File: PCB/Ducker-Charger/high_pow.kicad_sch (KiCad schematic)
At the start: 27 parts, among them Q1 NCE3080K, Q2 NCE3080K, Q3 NCE3080K, Q4 NCE3080K, U1 IP5389_CN_AACD_WC4QD

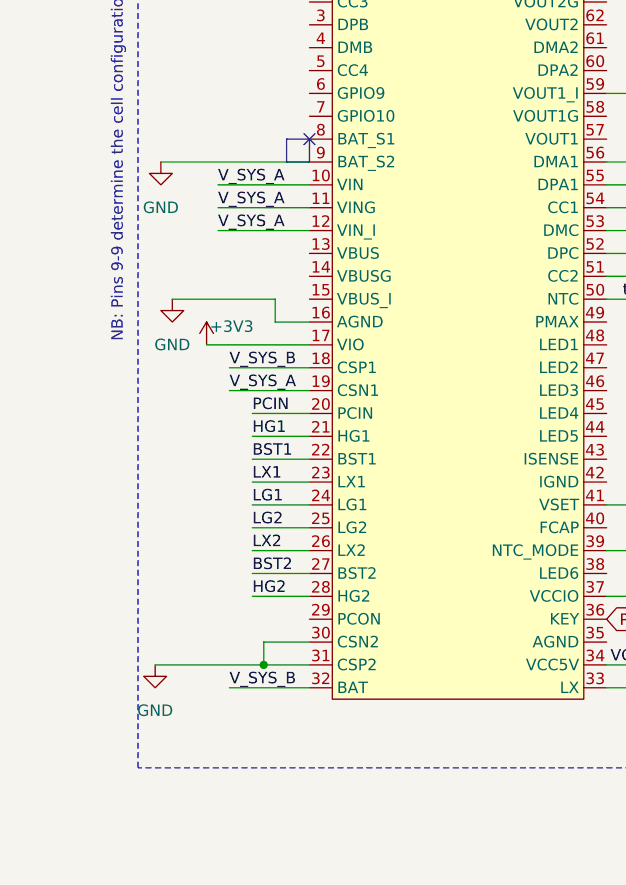
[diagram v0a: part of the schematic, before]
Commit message: feat: started BMS configuration
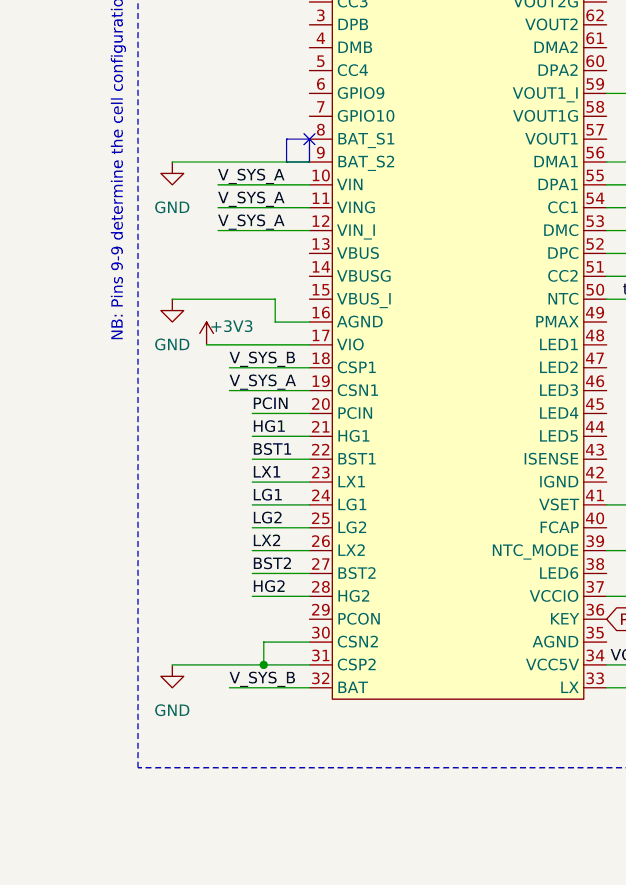
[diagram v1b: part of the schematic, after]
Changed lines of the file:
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@@
 	(wire
 		(pts
-			(xy 29.845 123.19) (xy 41.91 123.19)
+			(xy 31.75 123.19) (xy 41.91 123.19)
 		)
 		(stroke
@@
 	(wire
 		(pts
-			(xy 30.48 67.31) (xy 46.99 67.31)
+			(xy 31.75 67.31) (xy 46.99 67.31)
 		)
 		(stroke
@@
 	(symbol
 		(lib_id "power:GND")
-		(at 30.48 67.31 0)
+		(at 31.75 67.31 0)
 		(mirror y)
 		(unit 1)
@@
 		(fields_autoplaced yes)
 		(property "Reference" "#PWR018"
-			(at 30.48 73.66 0)
+			(at 31.75 73.66 0)
 			(effects
 				(font
@@
 		)
 		(property "Value" "GND"
-			(at 30.48 72.39 0)
+			(at 31.75 72.39 0)
 			(effects
 				(font
@@
 		)
 		(property "Footprint" ""
-			(at 30.48 67.31 0)
+			(at 31.75 67.31 0)
 			(effects
 				(font
@@
 		)
 		(property "Datasheet" ""
-			(at 30.48 67.31 0)
+			(at 31.75 67.31 0)
 			(effects
 				(font
@@
 		)
 		(property "Description" "Power symbol creates a global label with name \"GND\" , ground"
-			(at 30.48 67.31 0)
+			(at 31.75 67.31 0)
 			(effects
 				(font
@@
 	(symbol
 		(lib_id "power:GND")
-		(at 29.845 123.19 0)
+		(at 31.75 123.19 0)
 		(mirror y)
 		(unit 1)
@@
 		(fields_autoplaced yes)
 		(property "Reference" "#PWR019"
-			(at 29.845 129.54 0)
+			(at 31.75 129.54 0)
 			(effects
 				(font
@@
 		)
 		(property "Value" "GND"
-			(at 29.845 128.27 0)
+			(at 31.75 128.27 0)
 			(effects
 				(font
@@
 		)
 		(property "Footprint" ""
-			(at 29.845 123.19 0)
+			(at 31.75 123.19 0)
 			(effects
 				(font
@@
 		)
 		(property "Datasheet" ""
-			(at 29.845 123.19 0)
+			(at 31.75 123.19 0)
 			(effects
 				(font
@@
 		)
 		(property "Description" "Power symbol creates a global label with name \"GND\" , ground"
-			(at 29.845 123.19 0)
-			(effects
-				(font
+			(at 31.75 123.19 0)
+			(effects
+				(font

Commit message: feat: substituted IP5389 with BQ25713 + TPS25750
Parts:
- removed C_BST1, C_BST2: 100n, symbol Device:C
- removed R7: 51K, symbol Device:R
- removed TH1: Thermistor_NTC, symbol Device:Thermistor_NTC
- removed U1: IP5389_CN_AACD_WC4QD, EasyEDA:QFN-64_L8.0-W8.0-P0.40-TL-EP6.2, symbol EasyEDA:IP5389_CN_AACD_WC4QD
- added C32: 4.7u, symbol Device:C
- added C33: 1u, symbol Device:C
- added U7: TPS25750DRJKR, EasyEDA:QFN-38_L6.0-W4.0-P0.40-TL-EP_RJK, symbol EasyEDA:TPS25750DRJKR
- added U8: BQ25713RSNR, EasyEDA:QFN-32_L4.0-W4.0-P0.40-TL-EP2.8, symbol EasyEDA:BQ25713RSNR
- C1: value 10u -> 100n
- R2: value 27K -> 10
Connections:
- net GND: now also C32.2, C33.2, U8.27 (PGND), U8.33 (EP); no longer C1.2, C8.2, R2.2
- net SCL: now also U8.13 (SCL)
- net SDA: now also U8.12 (SDA)
- net VBUS: now also U8.1 (VBUS)
- net V_SYS_A: now also U8.20 (SRP), U8.22 (VSYS)
- net V_SYS_B: now also U8.19 (SRN)
- net CONF_SETT renamed REGN
- net REGN: now also C32.1, U8.28 (REGN)
- net HG1 renamed HIDRV2
- net HIDRV2: now also U8.24 (HIDRV2)
- net HG2 renamed HIDRV1
- net HIDRV1: now also U8.31 (HIDRV1)
- net LG1 renamed LODRV2
- net LODRV2: now also U8.26 (LODRV2)
- net LG2 renamed LODRV1
- net LODRV1: now also U8.29 (LODRV1)
- net LX1 renamed SW2
- net SW2: now also C8.2, U8.23 (SW2)
- net LX2 renamed SW1
- net SW1: now also C1.2, U8.32 (SW1)
- net PCIN renamed BTST2
- net BTST2: now also U8.25 (BTST2)
- net VCC5V renamed BTST1
- net BTST1: now also U8.30 (BTST1)
- new net VDDA: C33.1, R2.2, U8.7 (VDDA)
- no-connect marks 2 -> 1
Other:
- note removed: "BOOTSTRAP & DECOUPLING"
- note removed: "HARDWARE CONFIG"
- note removed: "HARDWARE SAFETY"
- note removed: "NB: Pins 9-9 determine the cell configuration"
- note removed: "pullup must be added 4k7 - 3v3"

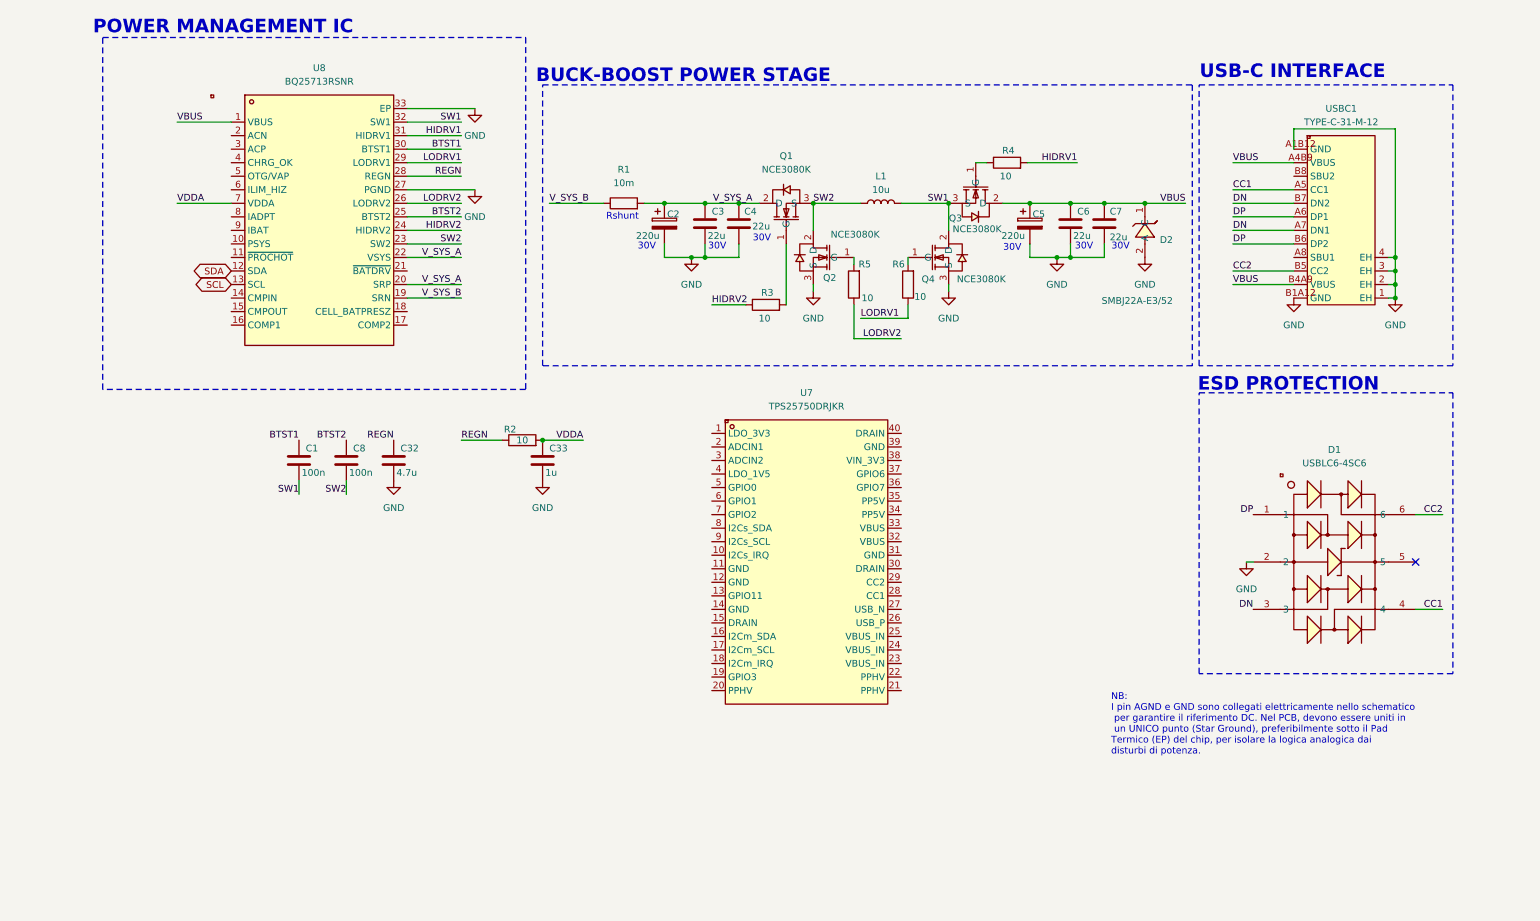
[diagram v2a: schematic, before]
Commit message: feat: completed BQ25713 + TPS25750 config
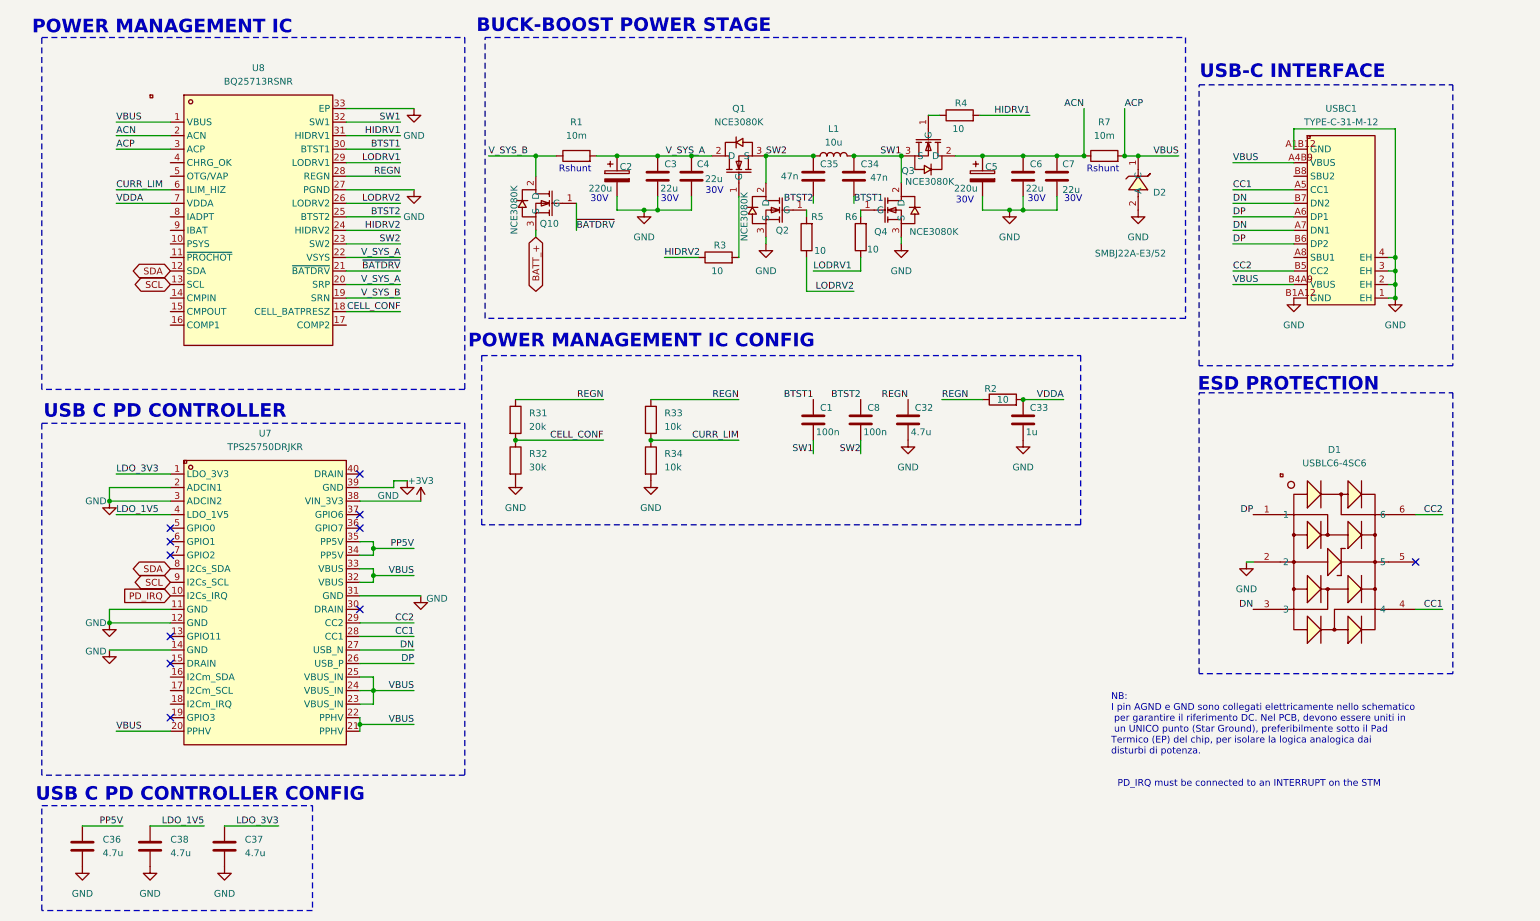
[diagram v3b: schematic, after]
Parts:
- added C34, C35: 47n, symbol Device:C
- added C36, C37, C38: 4.7u, symbol Device:C
- added Q10: NCE3080K, EasyEDA:TO-252-2_L6.6-W6.1-P4.57-LS9.9-TL-CW, symbol EasyEDA:NCE3080K
- added R31: 20k, symbol Device:R
- added R32: 30k, symbol Device:R
- added R33, R34: 10k, symbol Device:R
- added R7: 10m, symbol Device:R
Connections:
- net BTST1: now also C34.2
- net BTST2: now also C35.2
- net CC1: now also U7.28 (CC1)
- net CC2: now also U7.29 (CC2)
- net DN: now also U7.27 (USB_N)
- net DP: now also U7.26 (USB_P)
- net GND: now also U7.11 (GND), U7.12 (GND), U7.14 (GND), U7.2 (ADCIN1), U7.3 (ADCIN2), U7.31 (GND), U7.39 (GND), C36.2, C37.2, C38.2, R32.2, R34.2
- net REGN: now also R31.1, R33.1
- net SCL: now also U7.9 (I2Cs_SCL)
- net SDA: now also U7.8 (I2Cs_SDA)
- net SW1: now also C34.1
- net SW2: now also C35.1
- net V_SYS_B: now also Q10.2 (D)
- net CELL_CONF: now reaches U8.18 (CELL_BATPRESZ)
- net CELL_CONF: now also R31.2, R32.1
- net ACN: now reaches U8.2 (ACN)
- net ACN: now also C5.1, C6.1, C7.1, Q3.2 (D), R7.1
- net ~{BATDRV}: now reaches U8.21 (~{BATDRV})
- net ~{BATDRV}: now also Q10.1 (G)
- net ACP: now reaches U8.3 (ACP)
- net ACP: now also D2.1 (C), U7.20 (PPHV), U7.21 (PPHV), U7.22 (PPHV), U7.23 (VBUS_IN), U7.24 (VBUS_IN), U7.25 (VBUS_IN), U7.32 (VBUS), U7.33 (VBUS), U8.1 (VBUS), USBC1.A4B9 (VBUS), USBC1.B4A9 (VBUS), R7.2
- net CURR_LIM: now reaches U8.6 (ILIM_HIZ)
- net CURR_LIM: now also R33.2, R34.1
- net LDO_3V3: now reaches U7.1 (LDO_3V3)
- net LDO_3V3: now also C37.1
- net PD_IRQ: now reaches U7.10 (I2Cs_IRQ)
- net PP5V: now reaches U7.34 (PP5V)
- net PP5V: now also U7.35 (PP5V), C36.1
- net +3V3: now reaches U7.38 (VIN_3V3)
- net LDO_1V5: now reaches U7.4 (LDO_1V5)
- net LDO_1V5: now also C38.1
- removed net VBUS: C5.1, C6.1, C7.1, D2.1 (C), Q3.2 (D), U8.1 (VBUS), USBC1.A4B9 (VBUS), USBC1.B4A9 (VBUS)
- new net BATT_+: Q10.3 (S)
- no-connect marks 1 -> 11
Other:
- note added: "PD_IRQ must be connected to an INTERRUPT on the STM"
- note added: "POWER MANAGEMENT IC CONFIG"
- note added: "USB C PD CONTROLLER"
- note added: "USB C PD CONTROLLER CONFIG"
- moved on the sheet: C1, C2, C3, C32, C33, C4, C5, C6, C7, C8, D2, L1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

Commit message: feat: progressed overall schematic
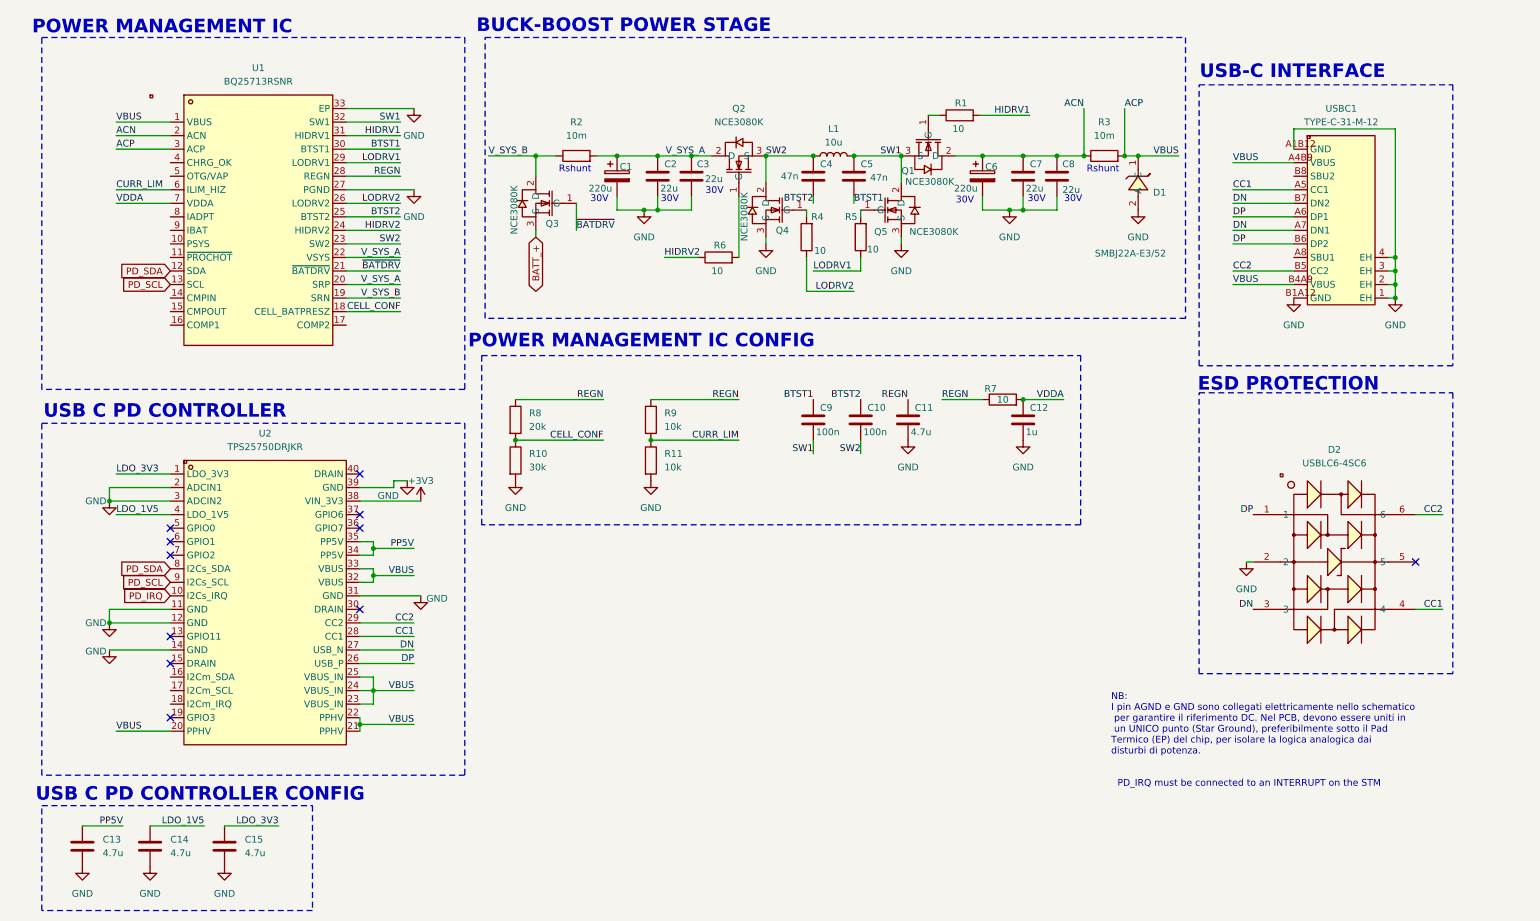
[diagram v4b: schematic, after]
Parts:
- renumbered C2 to C1, C8 to C10, C32 to C11, C33 to C12, C36 to C13, C38 to C14, C37 to C15, C3 to C2, C4 to C3, C35 to C4, C34 to C5, C5 to C6, C6 to C7, C7 to C8, C1 to C9, D2 to D1, D1 to D2, Q3 to Q1, Q1 to Q2, Q10 to Q3, Q2 to Q4, Q4 to Q5, R4 to R1, R32 to R10, R34 to R11, R1 to R2, R7 to R3, R5 to R4, R6 to R5, R3 to R6, R2 to R7, R31 to R8, R33 to R9, U8 to U1, U7 to U2
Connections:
- net SCL renamed PD_SCL
- net SDA renamed PD_SDA

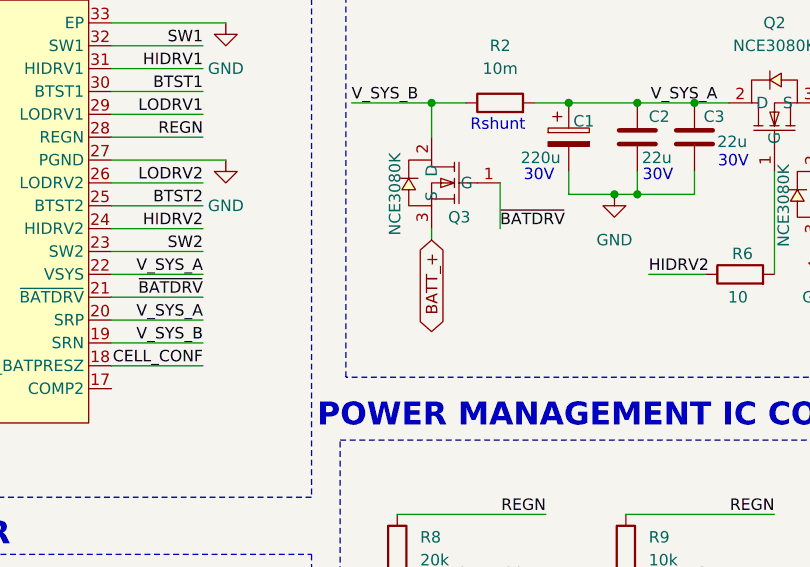
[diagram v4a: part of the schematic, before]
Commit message: fix: power symbols
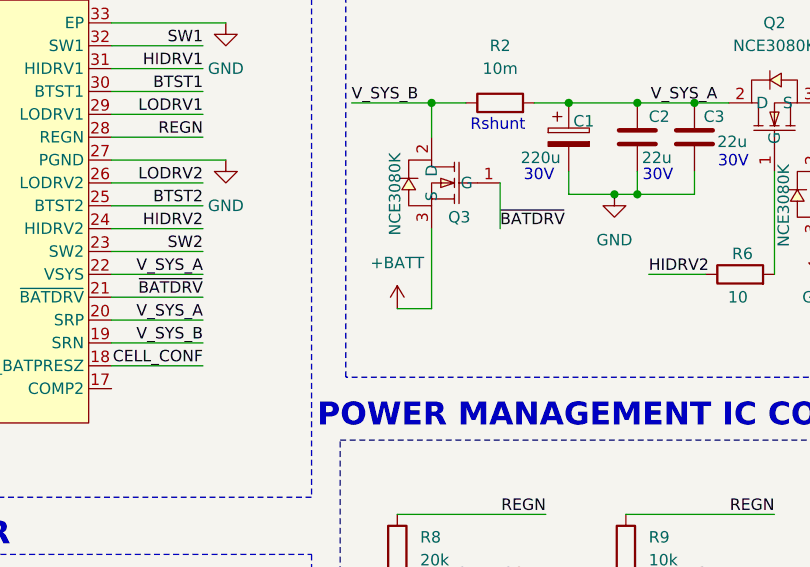
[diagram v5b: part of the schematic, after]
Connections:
- net BATT_+ renamed +BATT
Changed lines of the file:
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@@
+	(wire
+		(pts
+			(xy 109.22 74.93) (xy 105.41 74.93)
+		)
+		(stroke
+			(width 0)
+			(type default)
+		)
+	)
 	(wire
 		(pts
@@
 	(wire
 		(pts
+			(xy 109.22 66.04) (xy 109.22 74.93)
+		)
+		(stroke
+			(width 0)
+			(type default)
+		)
+	)
+	(wire
+		(pts
 			(xy 168.91 52.07) (xy 177.8 52.07)
 		)
@@
 		(pts
 			(xy 83.82 45.72) (xy 73.66 45.72)
-		)
-		(stroke
-			(width 0)
-			(type default)
-		)
-	)
-	(wire
-		(pts
-			(xy 109.22 66.04) (xy 109.22 67.31)
 		)
 		(stroke
@@
 		(property "Intersheetrefs" "${INTERSHEET_REFS}"
 			(at 30.6396 129.54 0)
-			(effects
-				(font
-					(size 1.27 1.27)
-				)
-				(justify right)
-				(hide yes)
-			)
-		)
-	)
-	(global_label "BATT_+"
-		(shape bidirectional)
-		(at 109.22 67.31 270)
-		(fields_autoplaced yes)
-		(effects
-			(font
-				(size 1.27 1.27)
-			)
-			(justify right)
-		)
-		(property "Intersheetrefs" "${INTERSHEET_REFS}"
-			(at 109.22 78.2403 90)
 			(effects
 				(font
@@
 					(unit 1)
 				)
+			)
+		)
+	)
+	(symbol
+		(lib_id "power:+BATT")
+		(at 105.41 74.93 0)
+		(unit 1)
+		(exclude_from_sim no)
+		(in_bom yes)
+		(on_board yes)
+		(dnp no)
+		(fields_autoplaced yes)
+		(property "Reference" "#PWR0111"
+			(at 105.41 78.74 0)
+			(effects
+				(font
+					(size 1.27 1.27)
+				)
+				(hide yes)
+			)
+		)
+		(property "Value" "+BATT"
+			(at 105.41 69.85 0)
+			(effects
+				(font
+					(size 1.27 1.27)
+				)
+			)
+		)
+		(property "Footprint" ""
+			(at 105.41 74.93 0)
+			(effects
+				(font
+					(size 1.27 1.27)
+				)
+				(hide yes)
+			)
+		)
+		(property "Datasheet" ""
+			(at 105.41 74.93 0)
+			(effects
+				(font
+					(size 1.27 1.27)
+				)
+				(hide yes)
+			)
+		)
+		(property "Description" "Power symbol creates a global label with name \"+BATT\""
+			(at 105.41 74.93 0)
+			(effects
+				(font
+					(size 1.27 1.27)
+				)
+				(hide yes)
+			)
+		)
+		(pin "1"
+		)
+		(instances
+			(project "Ducker-Charger"
+				(path "/74790d6c-a68e-4e6d-b4a9-43de1843f817/ccd240c6-b24b-451e-a22e-a82e757ea5cc"
+					(reference "#PWR0111")
+					(unit 1)
+				)
